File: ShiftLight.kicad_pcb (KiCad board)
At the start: 2 copper layers, 66.3 x 15.2 mm, 58 parts, among them J1 0533980471, J2 0533980571, U1 VOS618A, U2 LMR51406YDBV, U3 MSPM0C1104SDDFR, U4 TLC59208F, U5 VEML7700, U6 TLV803E

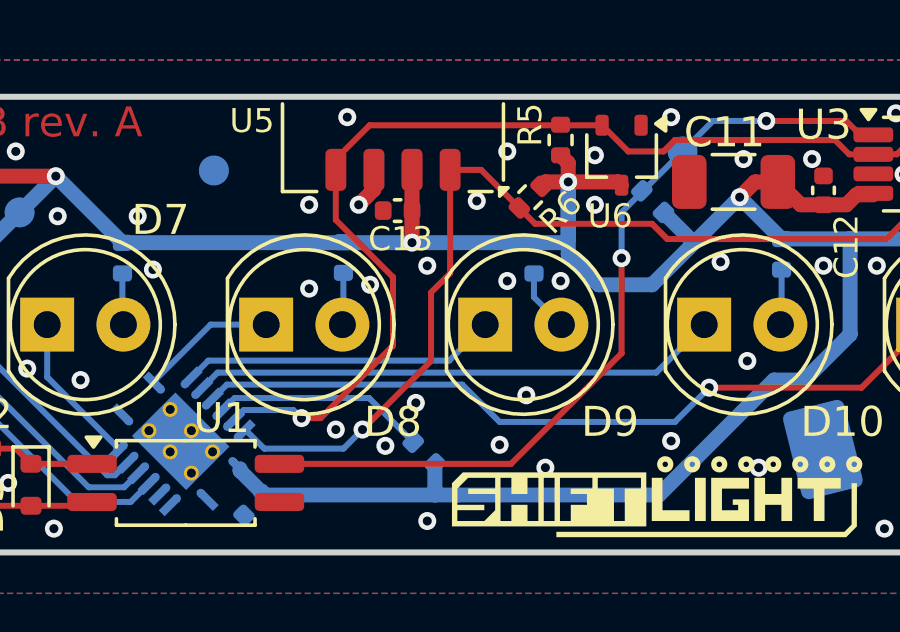
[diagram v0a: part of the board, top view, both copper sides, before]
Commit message: Fix swapped SCL and SDA pins for VEML7700
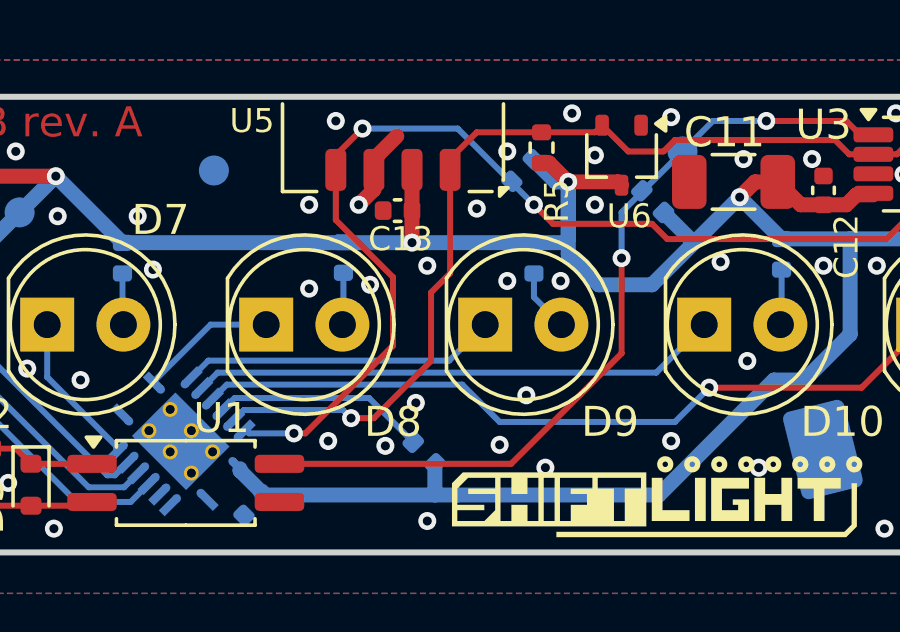
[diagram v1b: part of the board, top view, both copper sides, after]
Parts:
- R3: value 100k -> 68k
- R4: value 32k -> 22k
- R6: moved to B.Cu
- moved R6 0.92 mm to (120.3, 78.6)
- moved R5 0.68 mm to (120.9, 77.9)
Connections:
- U5 pad 1: /02_MCU/I2C_SDA -> /02_MCU/I2C_SCL
- U5 pad 4: /02_MCU/I2C_SCL -> /02_MCU/I2C_SDA
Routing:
- net /02_MCU/I2C_SDA: track 32.3 -> 36.0 mm, vias 1 -> 3
- net /02_MCU/I2C_SCL: track 54.7 -> 51.9 mm
- net GND: track 1.37 -> 2.81 mm, vias 83 -> 84
- net 3V3: track 128.7 -> 129.4 mm

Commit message: Layout: Increment revision to B
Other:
- board text added: "PCB rev. B"
- board text removed: "PCB rev. A"
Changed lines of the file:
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@@
 		(layer "Edge.Cuts")
 	)
-	(gr_text "PCB rev. A"
+	(gr_text "PCB rev. B"
 		(at 104.013 77.597 0)
 		(layer "F.Cu")

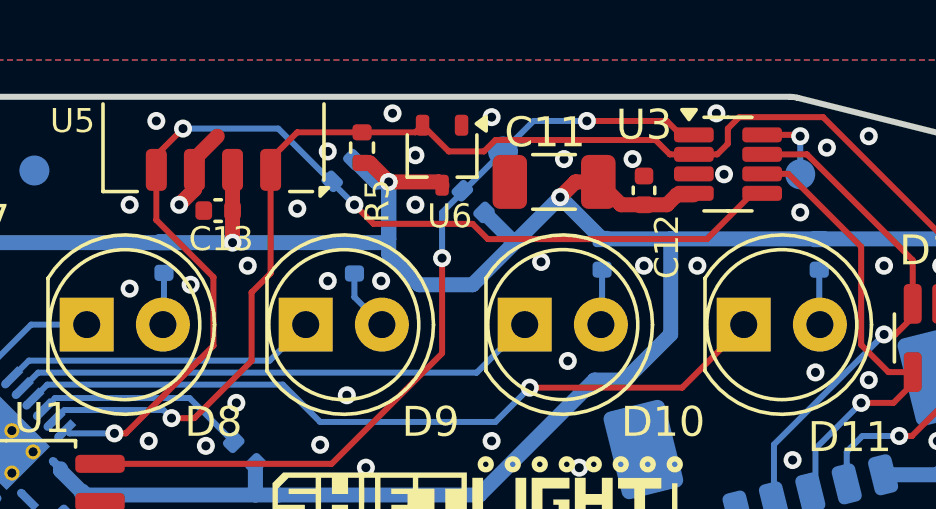
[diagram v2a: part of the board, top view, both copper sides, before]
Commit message: Fix wrong footprint for TLV803E
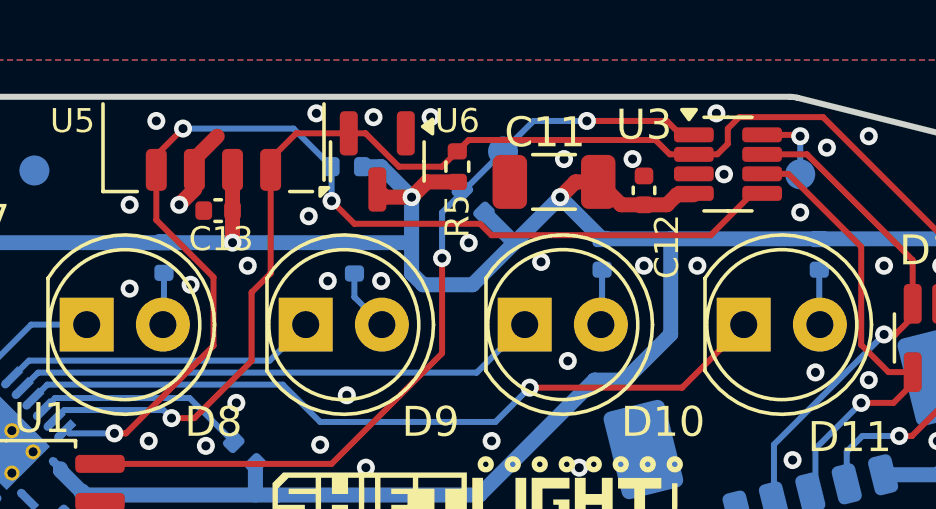
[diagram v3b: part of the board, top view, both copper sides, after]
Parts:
- U6: footprint Package_TO_SOT_SMD:SOT-323_SC-70 -> Package_TO_SOT_SMD:SOT-23
- moved R5 3.24 mm to (124.1, 78.5)
- moved U6 2.17 mm to (121.4, 78.3)
- moved R6 0.18 mm to (120.4, 78.5), turned to 180 degrees
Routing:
- net 3V3: track 129.4 -> 127.9 mm
- net /02_MCU/I2C_SDA: track 36.0 -> 36.6 mm
- net GND: vias 84 -> 83
